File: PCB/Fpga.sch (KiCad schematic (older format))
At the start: 59 parts

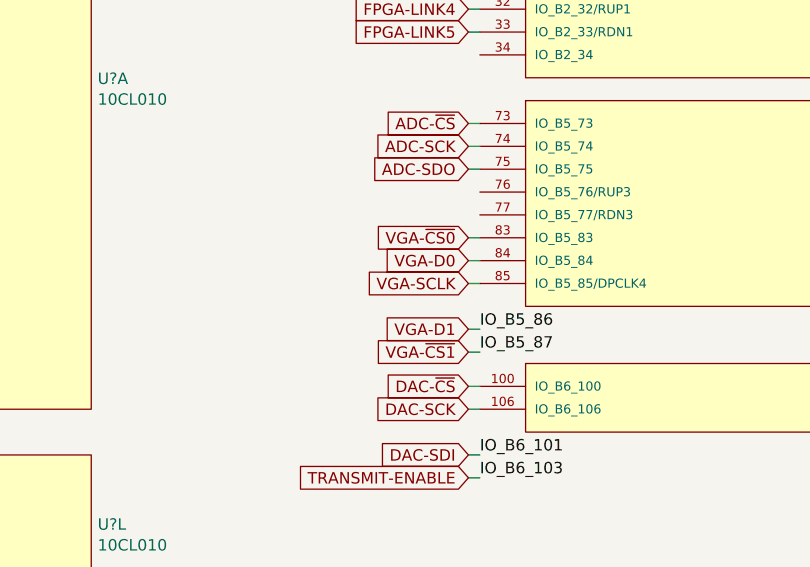
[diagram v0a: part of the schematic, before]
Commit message: Bring additional signals to the connectors sheet for debug access
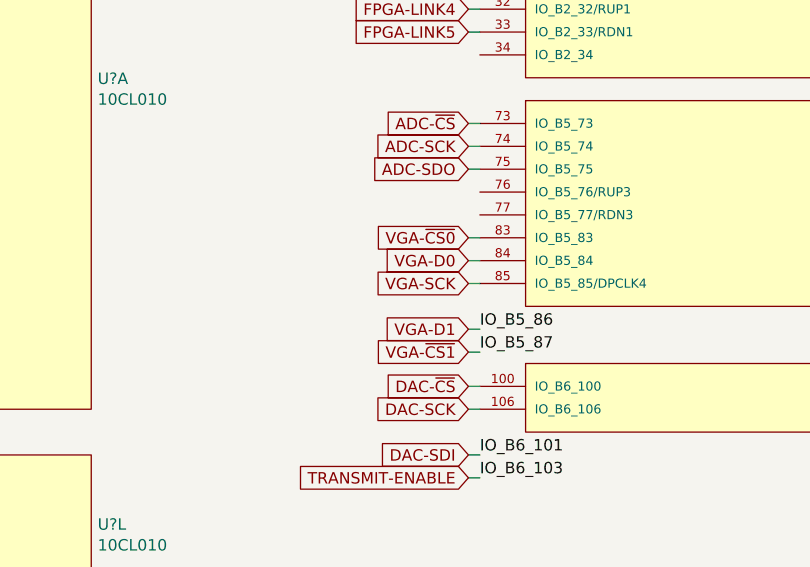
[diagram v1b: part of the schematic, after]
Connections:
- net VGA-SCLK renamed VGA-SCK
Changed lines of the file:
@@
 VGA-~CS1
 Text GLabel 4450 2850 0    50   Input ~ 0
-VGA-SCLK
+VGA-SCK
 Text GLabel 4450 2750 0    50   Input ~ 0
 VGA-D0

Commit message: Add missing footprints
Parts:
- NT?: footprint (none) -> Parts:NetTie-2
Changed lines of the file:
@@
 F 0 "NT?" H 1000 4381 50  0000 C CNN
 F 1 "Net-Tie_2" H 1000 4290 50  0000 C CNN
-F 2 "" H 1000 4200 50  0001 C CNN
+F 2 "Parts:NetTie-2" H 1000 4200 50  0001 C CNN
 F 3 "~" H 1000 4200 50  0001 C CNN
 	1    1000 4200

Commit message: Annotate schematic, simplify transmit circuit, shuffle receive opamp stages, reorder buttons so they match net names, reorder connectors to simplify routing, begin arranging parts on PCB
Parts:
- gave numbers to parts that had none: 52

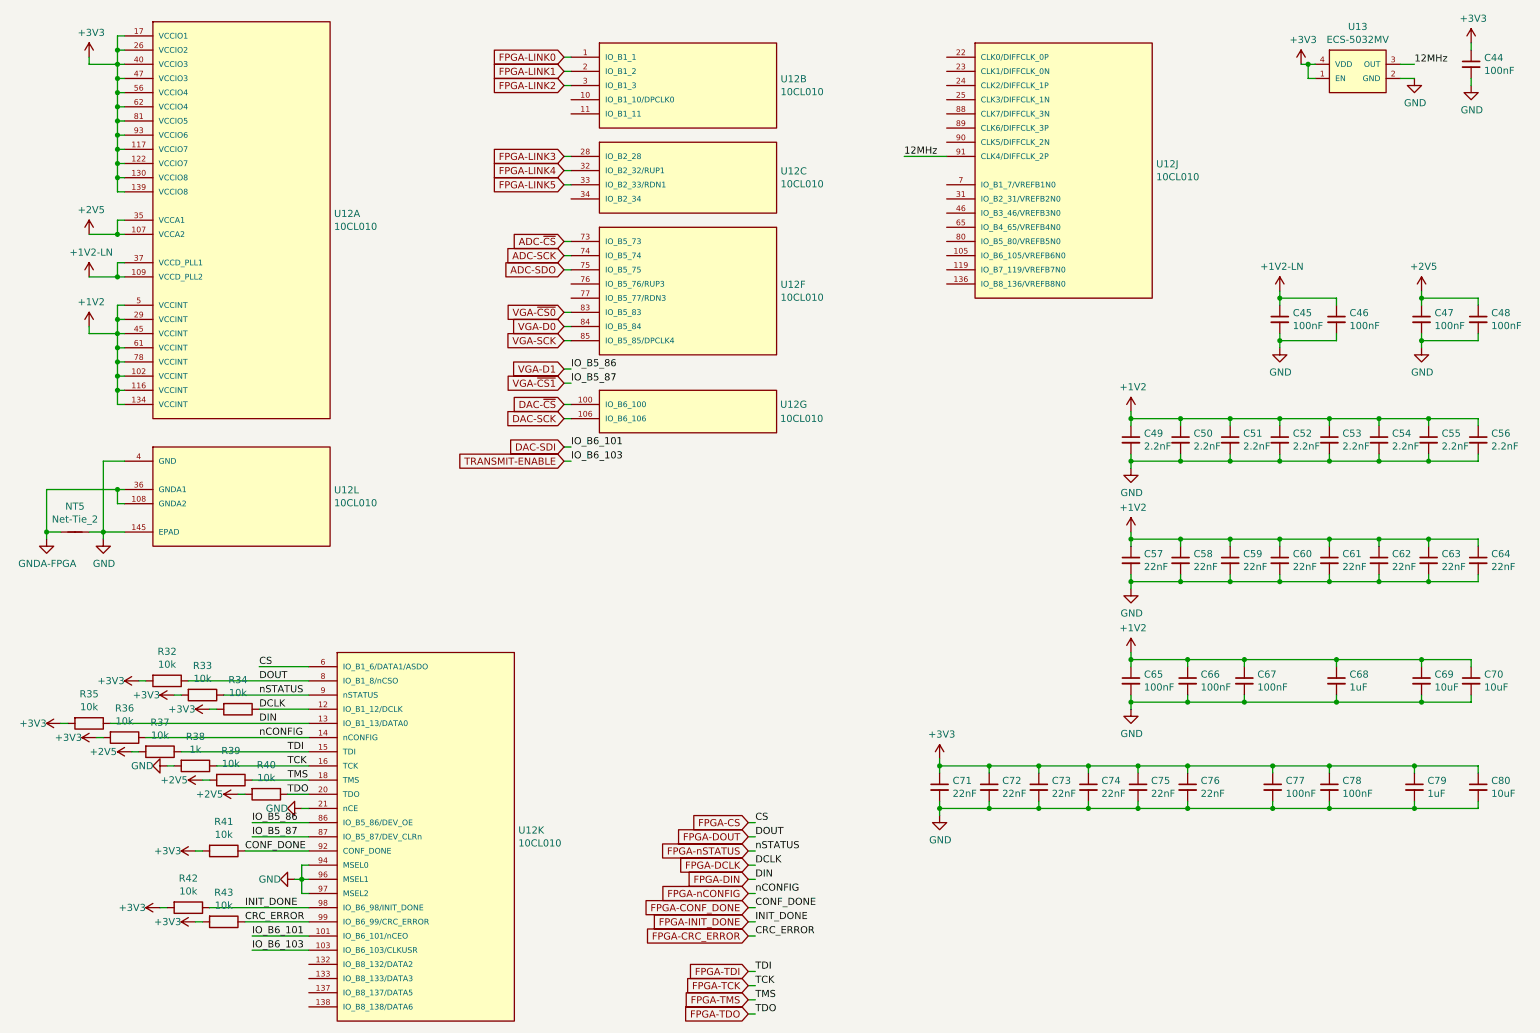
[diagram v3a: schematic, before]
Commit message: Begin layout around FPGA and microcontroller, rearrange some connections to FPGA and microcontroller, change groupings of optional debug pins
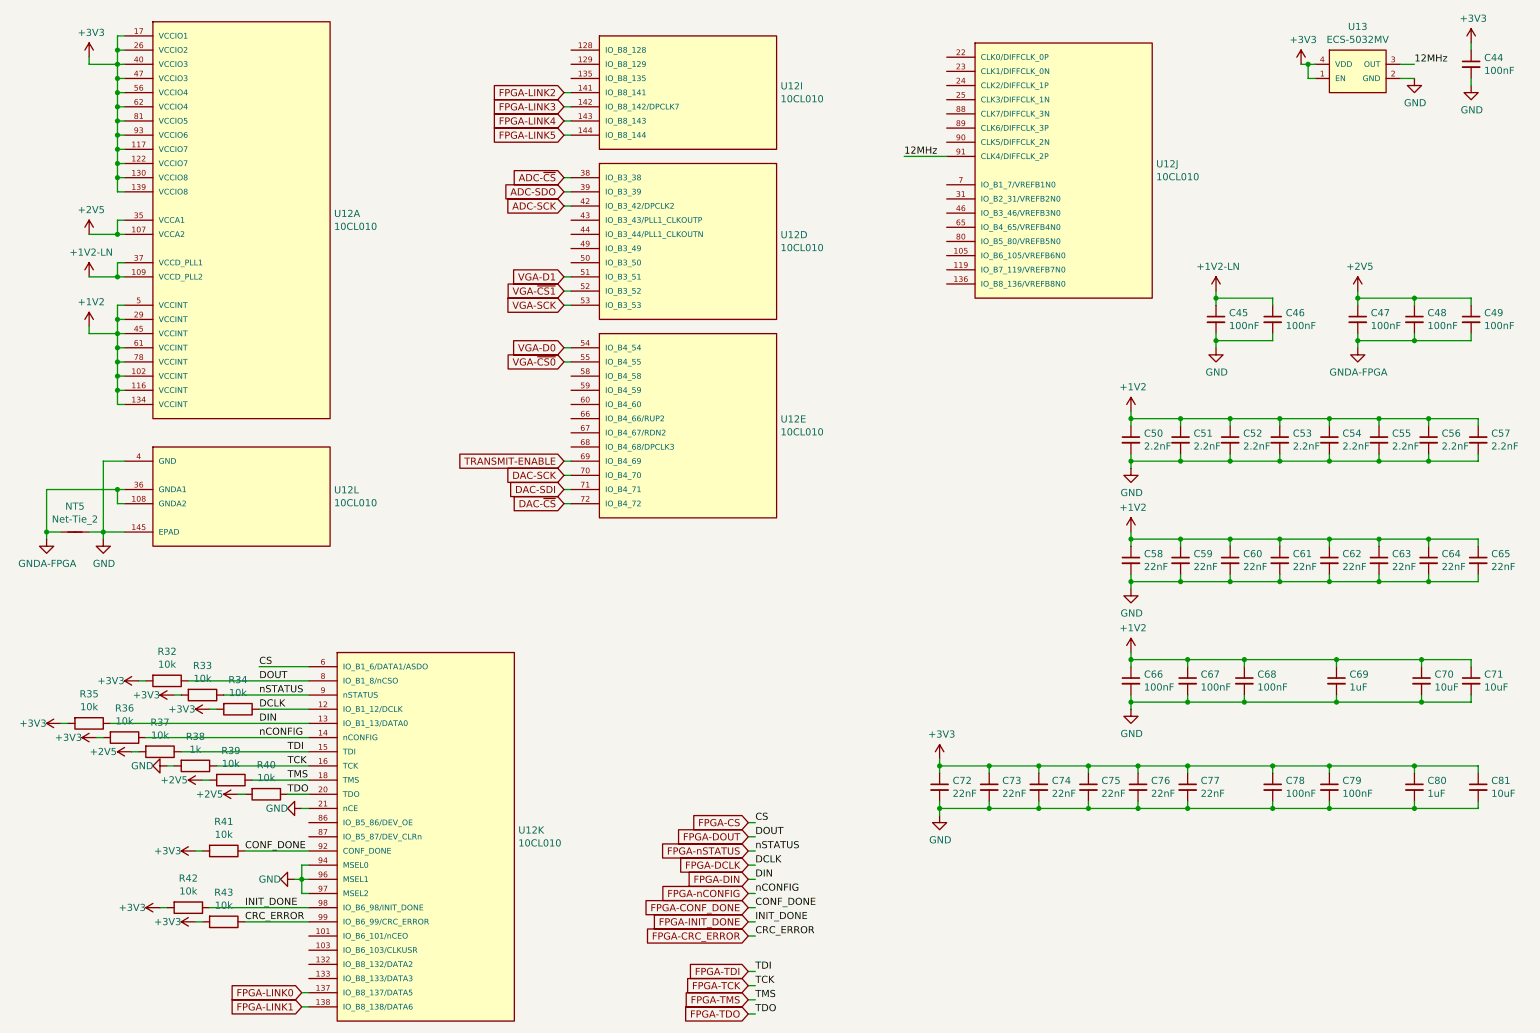
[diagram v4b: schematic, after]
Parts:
- removed unit 2 of U12
- removed unit 7 of U12
- removed unit 6 of U12
- removed unit 3 of U12
- added C49: 100nF, Capacitors_SMD:C_0603_HandSoldering, symbol Device:C_Small
- added unit 4 of U12
- added unit 5 of U12
- added unit 9 of U12
- renumbered C49 to C50, C50 to C51, C51 to C52, C52 to C53, C53 to C54, C54 to C55, C55 to C56, C56 to C57, C57 to C58, C58 to C59, C59 to C60, C60 to C61, C61 to C62, C62 to C63, C63 to C64, C64 to C65, C65 to C66, C66 to C67, C67 to C68, C68 to C69, C69 to C70, C70 to C71, C71 to C72, C72 to C73, C73 to C74, C74 to C75, C75 to C76, C76 to C77, C77 to C78, C78 to C79, C79 to C80, C80 to C81
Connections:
- net +2V5: now also C49.1
- net ADC-SCK: now also U12.42 (IO_B3_42/DPCLK2)
- net ADC-SDO: now also U12.39 (IO_B3_39)
- net ADC-~CS: now also U12.38 (IO_B3_38)
- net DAC-SCK: now also U12.70 (IO_B4_70)
- net DAC-SDI: now also U12.71 (IO_B4_71); no longer U12.101 (IO_B6_101/nCEO)
- net DAC-~CS: now also U12.72 (IO_B4_72)
- net FPGA-LINK0: now also U12.137 (IO_B8_137/DATA5)
- net FPGA-LINK1: now also U12.138 (IO_B8_138/DATA6)
- net FPGA-LINK2: now also U12.141 (IO_B8_141)
- net FPGA-LINK3: now also U12.142 (IO_B8_142/DPCLK7)
- net FPGA-LINK4: now also U12.143 (IO_B8_143)
- net FPGA-LINK5: now also U12.144 (IO_B8_144)
- net GND: no longer C47.2, C48.2
- net GNDA-FPGA: now also C47.2, C48.2, C49.2
- net TRANSMIT-ENABLE: now also U12.69 (IO_B4_69); no longer U12.103 (IO_B6_103/CLKUSR)
- net VGA-D0: now also U12.54 (IO_B4_54)
- net VGA-D1: now also U12.51 (IO_B3_51); no longer U12.86 (IO_B5_86/DEV_OE)
- net VGA-SCK: now also U12.53 (IO_B3_53)
- net VGA-~CS0: now also U12.55 (IO_B4_55)
- net VGA-~CS1: now also U12.52 (IO_B3_52); no longer U12.87 (IO_B5_87/DEV_CLRn)
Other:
- moved on the sheet: C45, C46, C47, C48

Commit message: Remove unnecessary series resistors, rearrange connections on FPGA and microcontroller, rearrange debug pins, layout most of FPGA and microcontroller sections
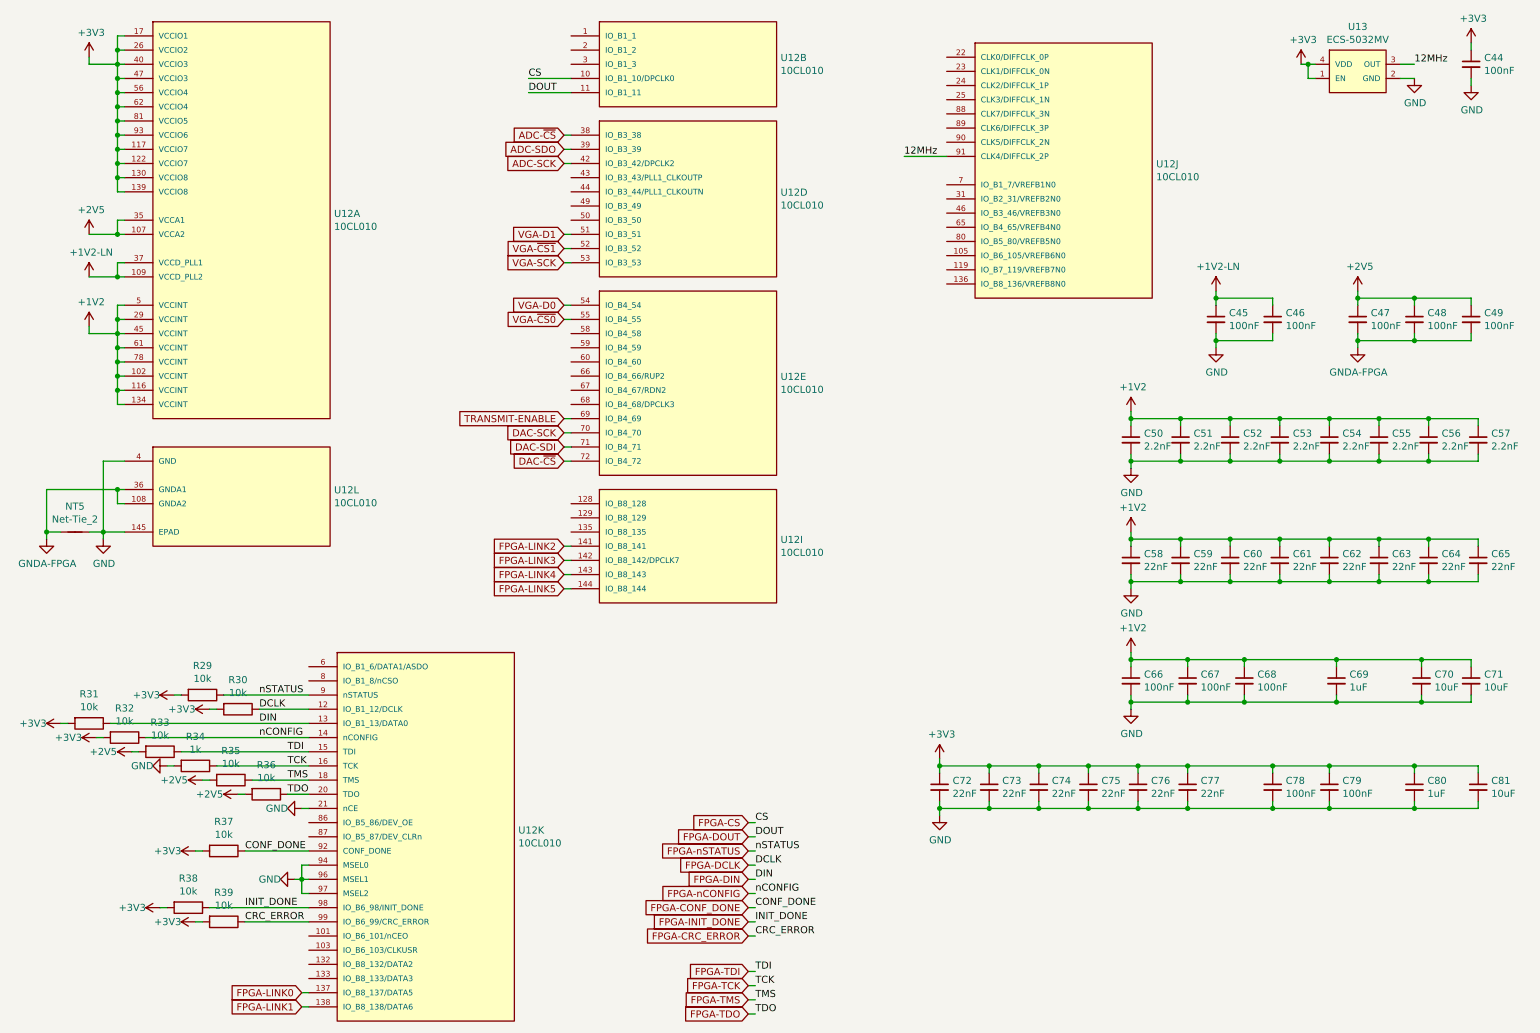
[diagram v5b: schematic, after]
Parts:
- removed R32: 10k, Resistors_SMD:R_0603_HandSoldering, symbol Device:R
- added unit 2 of U12
- renumbered R33 to R29, R34 to R30, R35 to R31, R36 to R32, R37 to R33, R38 to R34, R39 to R35, R40 to R36, R41 to R37, R42 to R38, R43 to R39
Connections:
- net FPGA-CS: now also U12.10 (IO_B1_10/DPCLK0); no longer U12.6 (IO_B1_6/DATA1/ASDO)
- net FPGA-DOUT: now also U12.11 (IO_B1_11); no longer U12.8 (IO_B1_8/nCSO)
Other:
- moved on the sheet: U12D, U12E, U12I

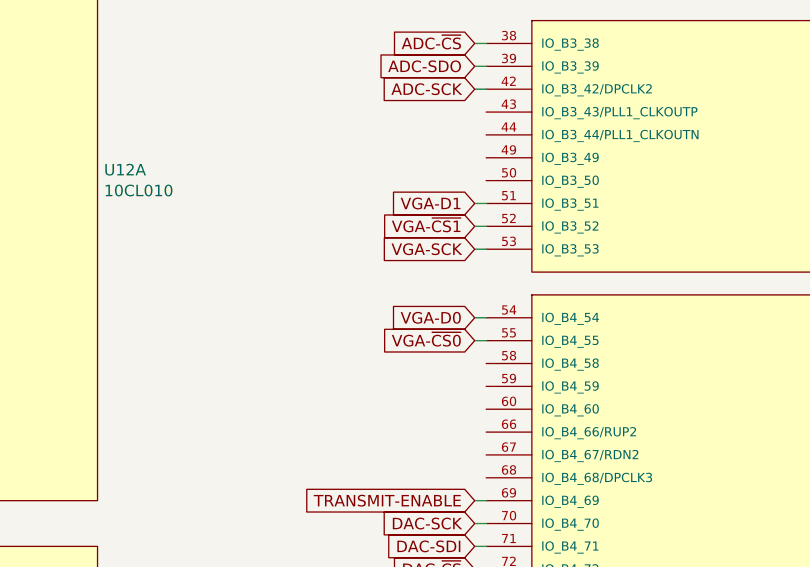
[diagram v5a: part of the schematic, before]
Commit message: Rearrange FPGA connections, combine VGA and ADC debug headers, layout most of VGA and ADC circuits
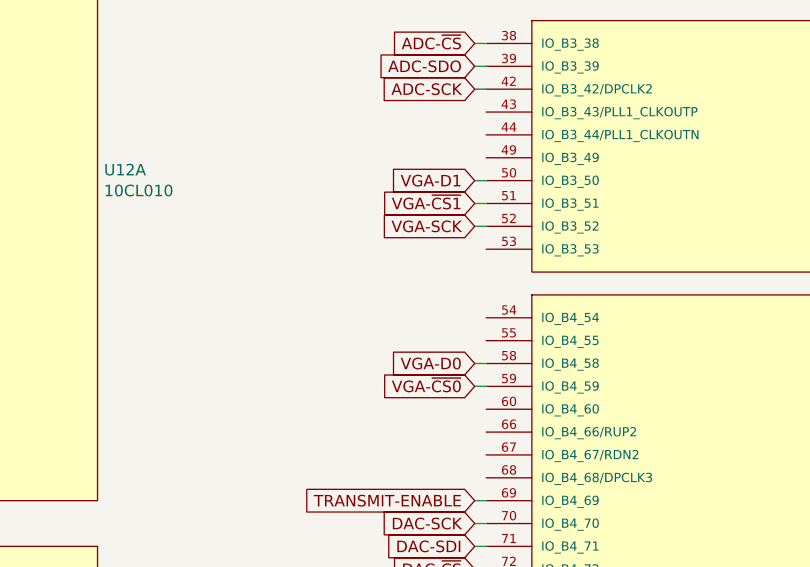
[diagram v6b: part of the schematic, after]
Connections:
- net VGA-D0: now also U12.58 (IO_B4_58); no longer U12.54 (IO_B4_54)
- net VGA-D1: now also U12.50 (IO_B3_50); no longer U12.51 (IO_B3_51)
- net VGA-SCK: now also U12.52 (IO_B3_52); no longer U12.53 (IO_B3_53)
- net VGA-~CS0: now also U12.59 (IO_B4_59); no longer U12.55 (IO_B4_55)
- net VGA-~CS1: now also U12.51 (IO_B3_51); no longer U12.52 (IO_B3_52)
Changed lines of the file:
@@
 Text GLabel 4450 3400 0    50   Input ~ 0
 TRANSMIT-ENABLE
-Text GLabel 4450 2700 0    50   Input ~ 0
+Text GLabel 4450 2900 0    50   Input ~ 0
 VGA-~CS0
+Text GLabel 4450 2100 0    50   Input ~ 0
+VGA-~CS1
 Text GLabel 4450 2200 0    50   Input ~ 0
-VGA-~CS1
-Text GLabel 4450 2300 0    50   Input ~ 0
 VGA-SCK
-Text GLabel 4450 2600 0    50   Input ~ 0
+Text GLabel 4450 2800 0    50   Input ~ 0
 VGA-D0
-Text GLabel 4450 2100 0    50   Input ~ 0
+Text GLabel 4450 2000 0    50   Input ~ 0
 VGA-D1
 $Comp
@@
 	4450 3400 4500 3400
 Wire Wire Line
-	4450 2700 4500 2700
+	4450 2900 4500 2900
 Wire Wire Line
-	4500 2600 4450 2600
-Wire Wire Line
-	4450 2300 4500 2300
+	4500 2800 4450 2800
 Wire Wire Line
 	4450 2200 4500 2200
@@
 	4450 2100 4500 2100
 Wire Wire Line
+	4450 2000 4500 2000
+Wire Wire Line
 	4450 1600 4500 1600
